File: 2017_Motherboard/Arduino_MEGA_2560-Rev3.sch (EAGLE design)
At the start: 60 parts, among them IC1 NCP1117ST50T3G, IC3 ATMEGA2560-16AU, IC7 LMV358IDGKR, X1 POWERSUPPLY_DC21MMX, Y1 CSTCE16M0V53-R0 16MHZ

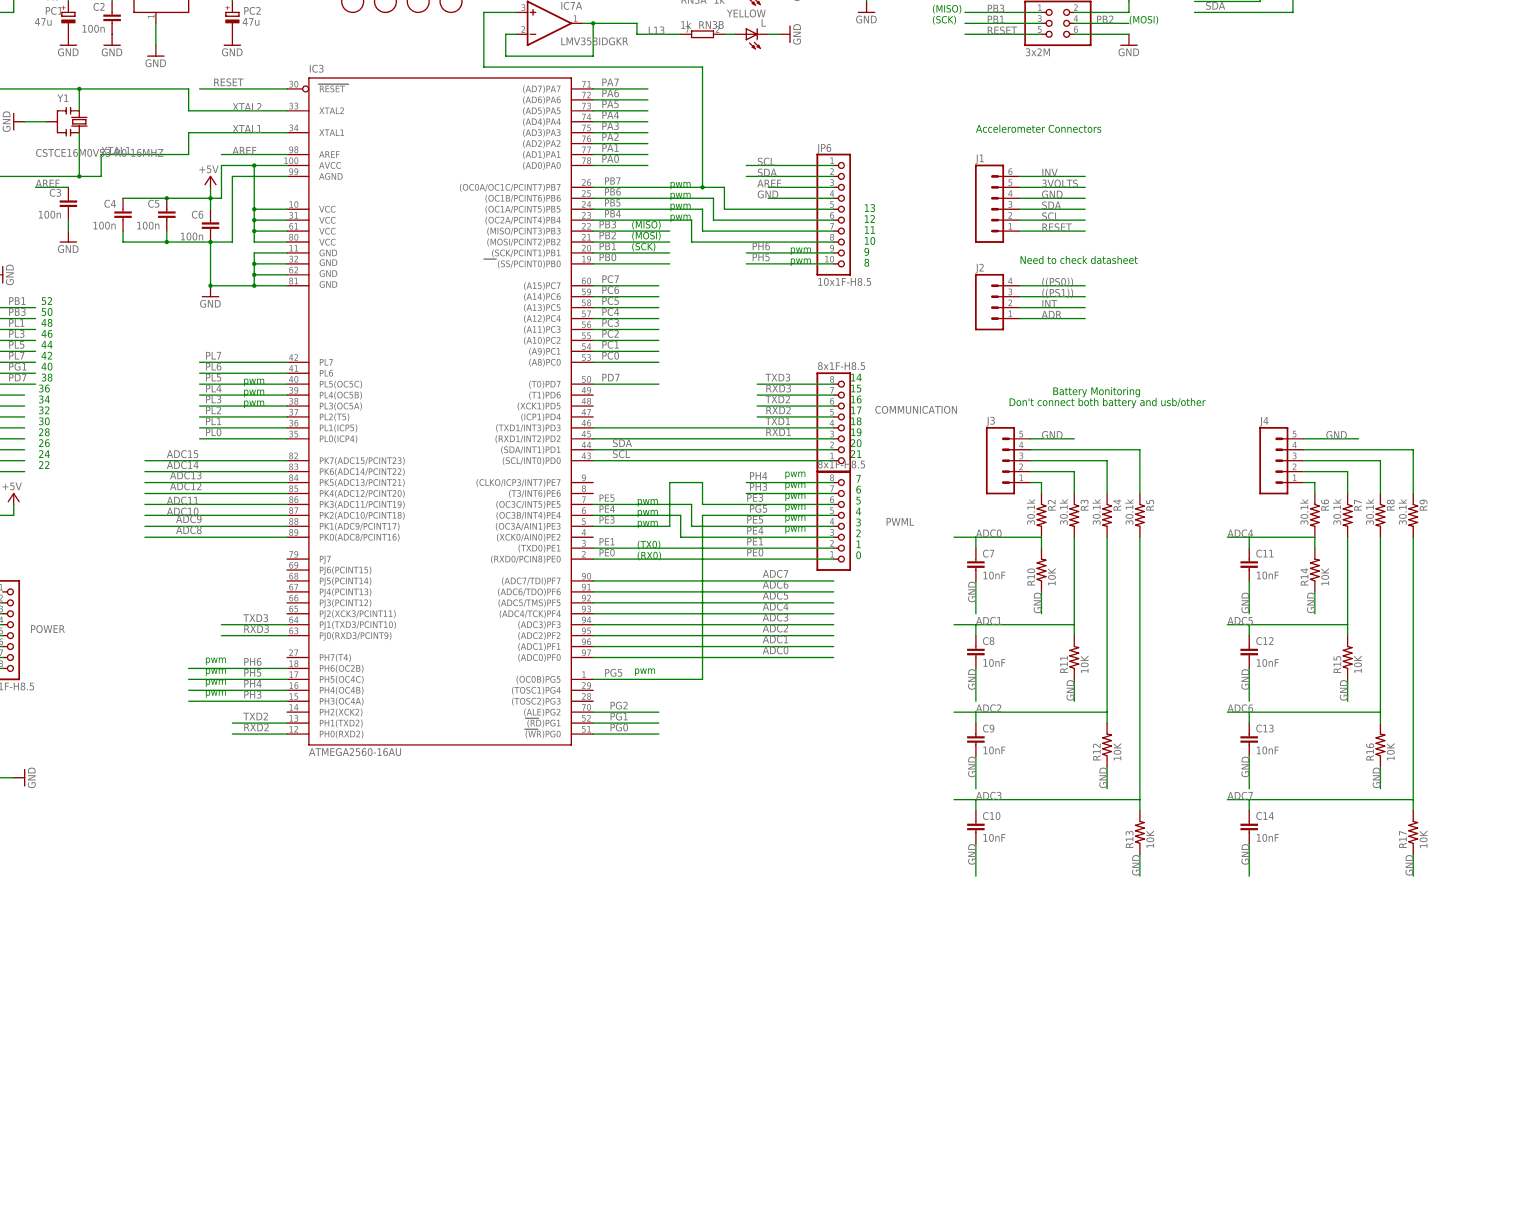
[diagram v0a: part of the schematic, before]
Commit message: Motherboard accelerometer + FTDI
updated to current FTDI and accelerometer on the schematic
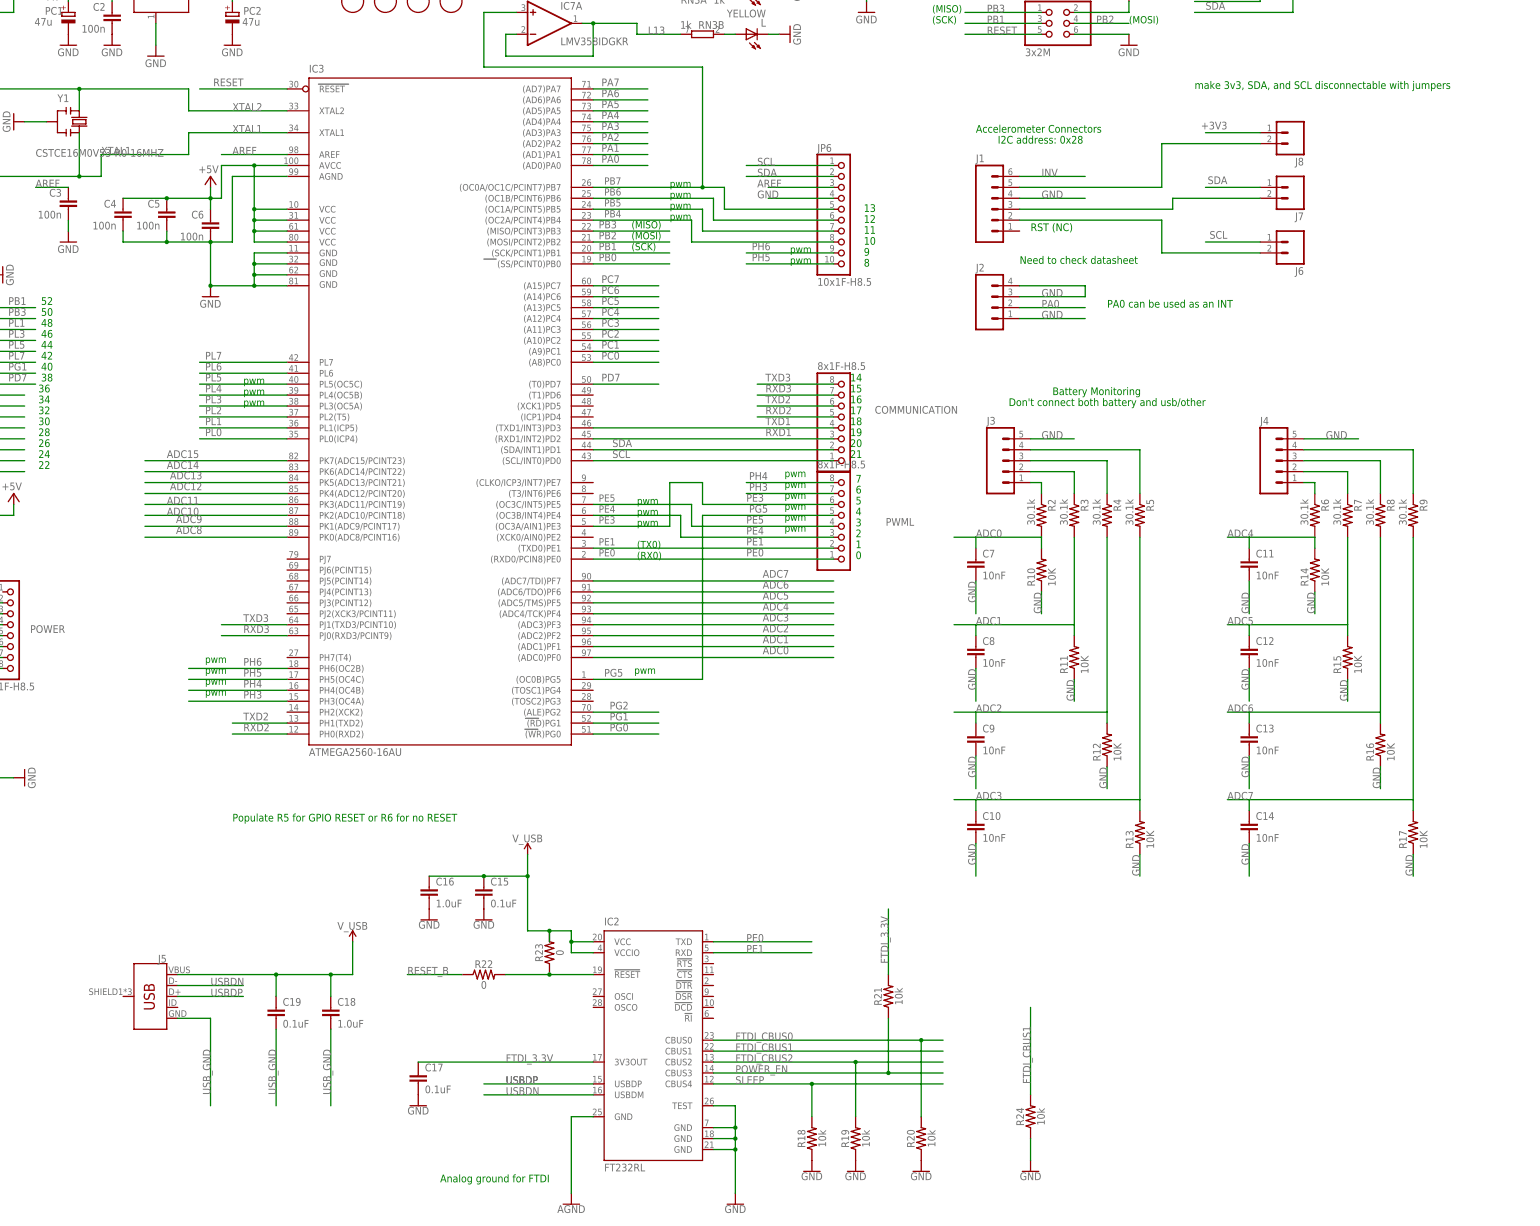
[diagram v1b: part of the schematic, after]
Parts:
- added C15, C17, C19: 0.1uF, SparkFun-Capacitors:0.1UF-0603-25V-5%
- added C16, C18: 1.0uF, SparkFun-Capacitors:1.0UF-0603-16V-10%
- added IC2: FT232RL, ftdichip:FT232RL
- added J5: (no value), SparkFun-Connectors:USB_MICRO-B_FEMALE-SMT
- added J6, J7, J8: (no value), SparkFun-Connectors:M02PTH
- added R18, R19, R20, R21, R24: 10k, SparkFun-Resistors:10KOHM-0603-1/10W-1%
- added R22, R23: 0, SparkFun-Resistors:0OHM-0603-1/10W-5%
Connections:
- removed net ((PS0)): J2.4
- removed net ((PS1)): J2.3
- removed net 3VOLTS: J1.5
- removed net ADR: J2.1
- removed net INT: J2.2
- new net AGND: IC2.GND@A
- new net FTDI_3.3V: C17.1, IC2.3V3OUT, R21.2
- new net FTDI_CBUS0: IC2.CBUS0, R20.2
- new net FTDI_CBUS1: IC2.CBUS1, R24.2
- new net FTDI_CBUS2: IC2.CBUS2, R19.2
- new net N$11: J1.2, J6.2
- new net N$4: IC2.!RESET, R22.2, R23.1
- new net N$7: J1.5, J8.2
- new net N$9: J1.3, J7.2
- new net POWER_EN: IC2.CBUS3, R21.1
- new net RESET_B: R22.1
- new net SLEEP: IC2.CBUS4, R18.2
- new net USBDN: IC2.USBDM, J5.D-
- new net USBDP: IC2.USBDP, J5.D+
- new net USB_GND: C18.2, C19.2, J5.GND
- new net V_USB: C15.1, C16.1, C18.1, C19.1, IC2.VCC, IC2.VCCIO, J5.VBUS
- net +3V3: now also J8.1
- net GND: now also C15.2, C16.2, C17.2, IC2.GND, IC2.GND@1, IC2.GND@2, IC2.TEST, J2.1, J2.3, J2.4, R18.1, R19.1, R20.1, R24.1
- net PA0: now also J2.2
- net PE0: now also IC2.TXD
- net PE1: now also IC2.RXD
- net RESET: no longer J1.1
- net SCL: now also J6.1; no longer J1.2
- net SDA: now also J7.1; no longer J1.3
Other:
- note added: "Analog ground for FTDI"
- note added: "I2C address: 0x28"
- note added: "PA0 can be used as an INT"
- note added: "Populate R5 for GPIO RESET or R6 for no RESET"
- note added: "RST (NC)"
- note added: "make 3v3, SDA, and SCL disconnectable with jumpers"

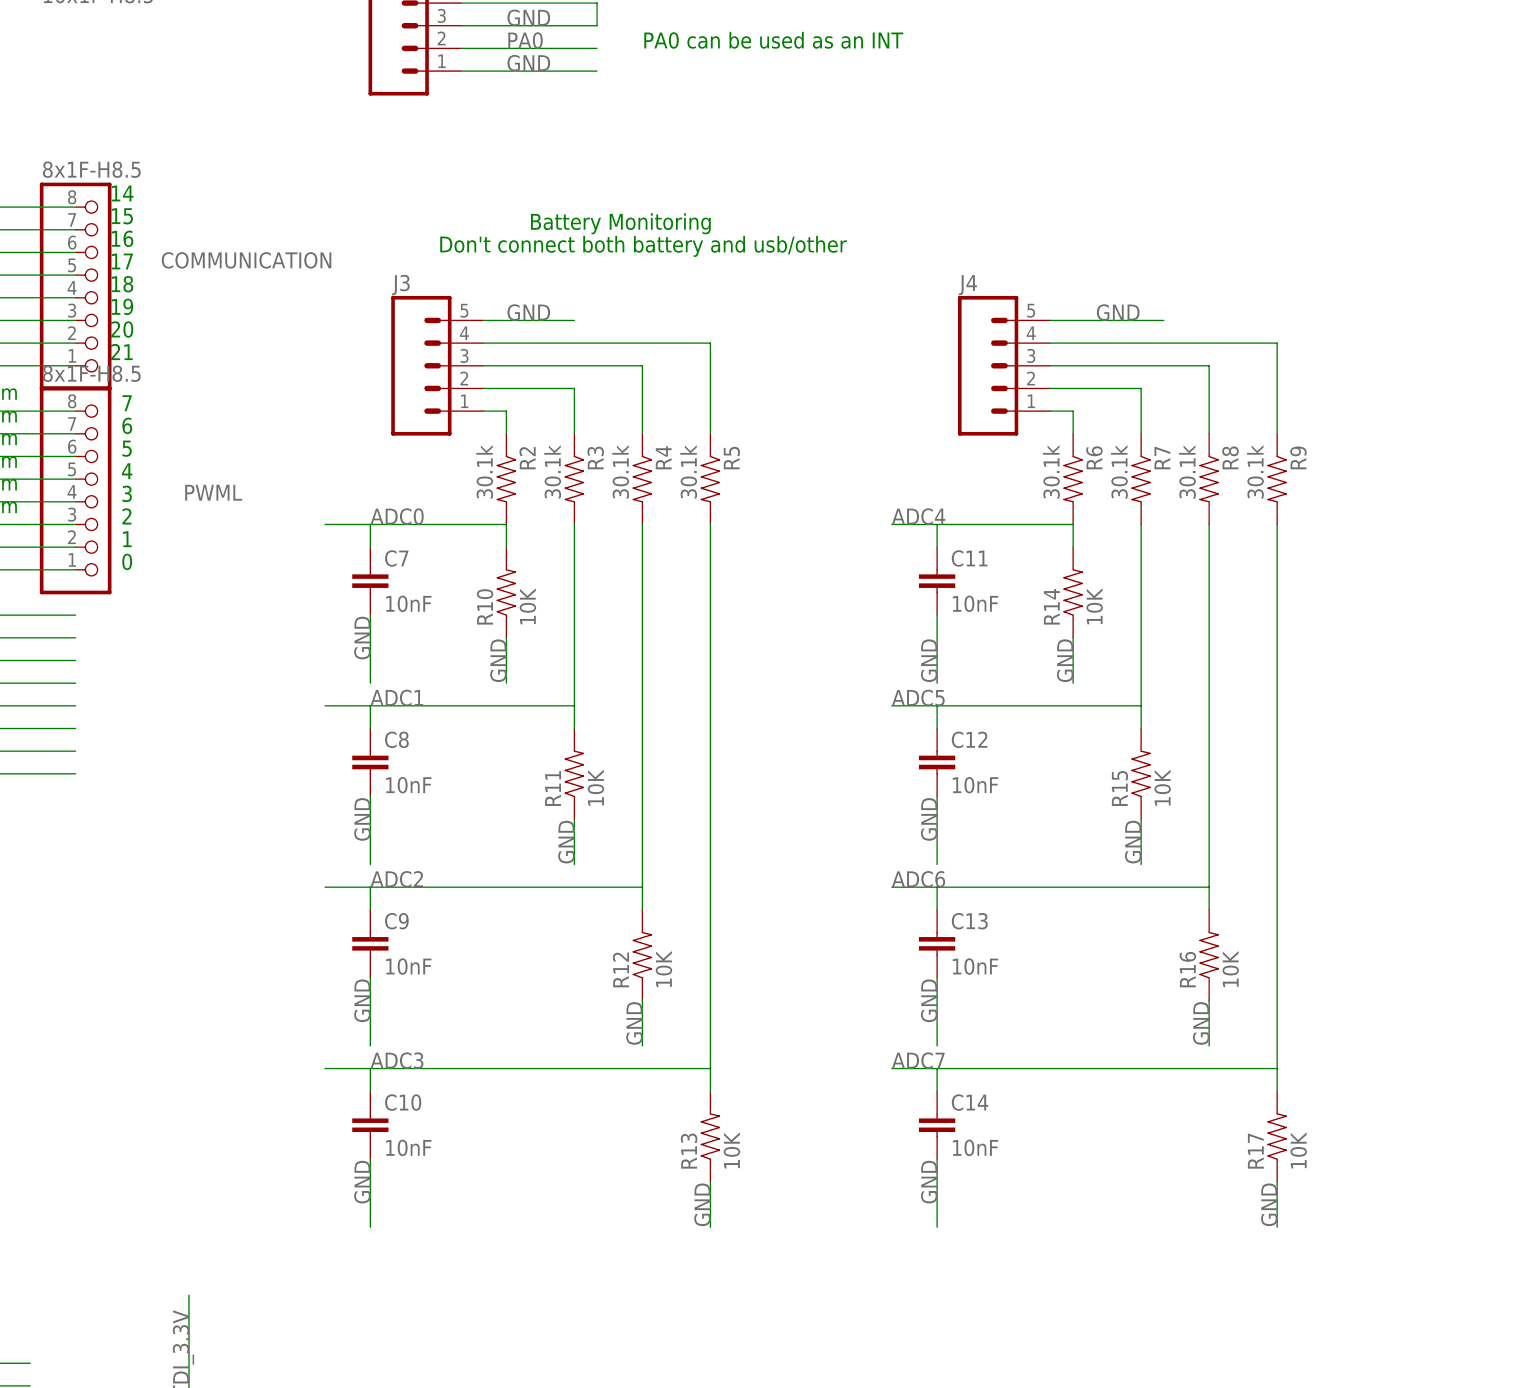
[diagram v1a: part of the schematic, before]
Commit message: Added GND for PWMs
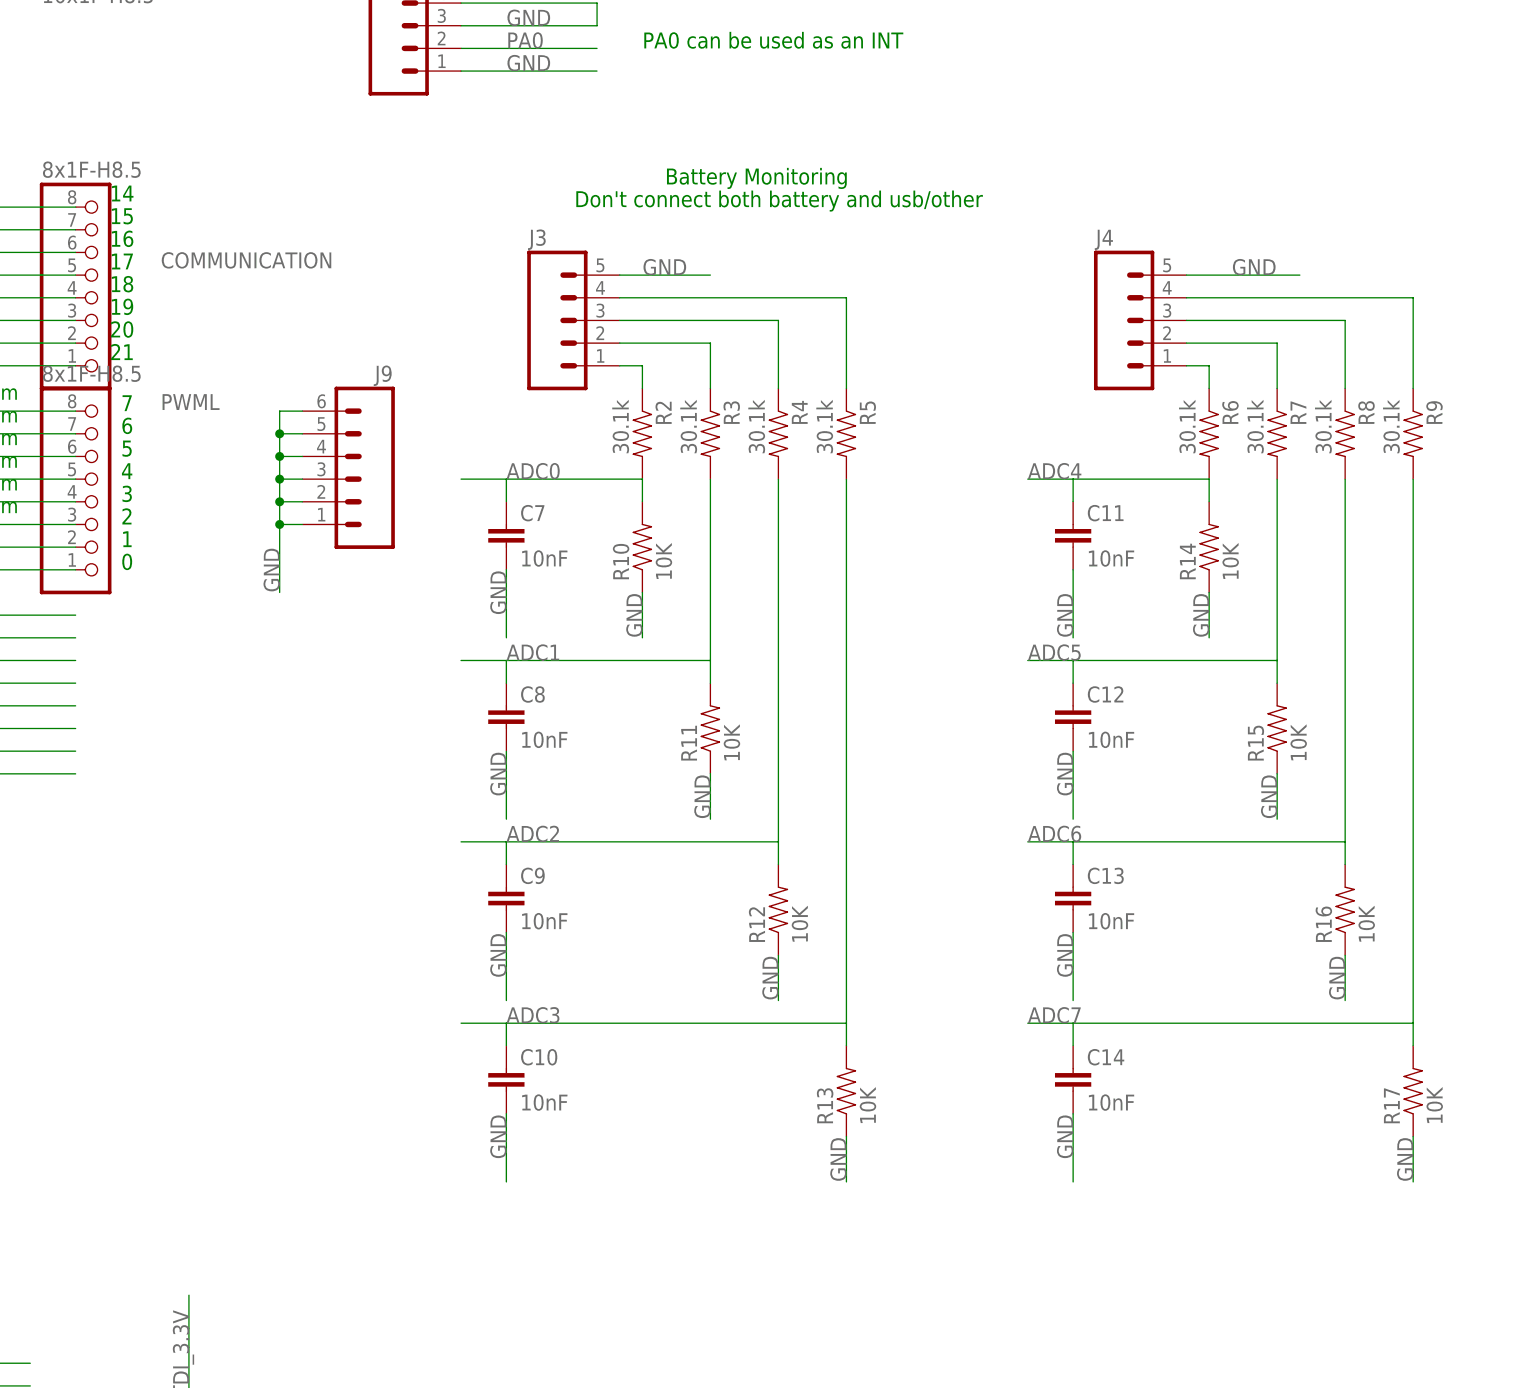
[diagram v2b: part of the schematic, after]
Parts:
- added J9: (no value), SparkFun-Connectors:M06LONGPADS
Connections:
- net GND: now also J9.1, J9.2, J9.3, J9.4, J9.5, J9.6
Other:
- moved on the sheet: C10, C11, C12, C13, C14, C7, C8, C9, J3, J4, R10, R11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
